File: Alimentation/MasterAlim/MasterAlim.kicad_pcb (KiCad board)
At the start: 2 copper layers, 84 parts, among them J1 Ext-Con, J10 Interf-Reg1, J11 AU Logic, J12 Interf-Reg2, J13 Interf-Reg3, J14 Interf-Reg4, J3 Bat. IN, J5 Direct Out, J6 Reg 1, J7 Reg 2, J8 Reg 3, J9 Reg 4, U1 74LS33, U2 PCF8591, U3 ACS712xLCTR-20A, U4 PCF8591, U5 PCF8591, U6 PTN78020W_EUK-7, U7 ACS712xLCTR-20A, U8 PCF8574A

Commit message: Dimensionnement et récupération des part LCSC
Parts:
- added C12: 1u, Capacitor_SMD:CP_Elec_4x5.3, F.Cu at (155.9, 131.8)
- added C14: 1n, Capacitor_SMD:C_0603_1608Metric_Pad1.08x0.95mm_HandSolder, F.Cu at (41.0, 36.5)
- added C16: 2.2u, Capacitor_SMD:C_0805_2012Metric_Pad1.18x1.45mm_HandSolder, F.Cu at (35.5, 48.5)
- added C17: 330u, Capacitor_SMD:CP_Elec_10x10, F.Cu at (38.5, 95.0)
- added C19: 1n, Capacitor_SMD:C_0603_1608Metric_Pad1.08x0.95mm_HandSolder, F.Cu at (162.5, 115.0)
- added C4: 1u, Capacitor_SMD:CP_Elec_4x5.3, F.Cu at (186.0, 123.5)
- added J2: 5V, TerminalBlock_Phoenix:TerminalBlock_Phoenix_MPT-0,5-6-2.54_1x06_P2.54mm_Horizontal, F.Cu at (34.0, 106.0)
- added REF**: MountingHole_3.2mm_M3, MountingHole:MountingHole_3.2mm_M3, F.Cu at (24.0, 106.0)
- added REF**: MountingHole_3.2mm_M3, MountingHole:MountingHole_3.2mm_M3, F.Cu at (24.0, 24.0)
- C1, C6, C9: footprint Capacitor_SMD:CP_Elec_3x5.3 -> Capacitor_SMD:CP_Elec_8x6.5
- C10, C13, C15, C18, C2, C5, C7: footprint Capacitor_SMD:C_0805_2012Metric -> Capacitor_SMD:C_0805_2012Metric_Pad1.18x1.45mm_HandSolder
- J10, J12, J13, J14: footprint Connector_JST:JST_EH_S5B-EH_1x05_P2.50mm_Horizontal -> Connector_JST:JST_PH_B5B-PH-K_1x05_P2.00mm_Vertical
- R1, R10, R11, R12, R13, R14, R15, R16, R17, R18, R19, R20, R21, R22, R23, R24, R25, R26, R27, R3, R8, R9: footprint Resistor_SMD:R_0805_2012Metric -> Resistor_SMD:R_0805_2012Metric_Pad1.20x1.40mm_HandSolder
- R2: value 150 -> 220; footprint Resistor_SMD:R_0805_2012Metric -> Resistor_SMD:R_0805_2012Metric_Pad1.20x1.40mm_HandSolder
- R28: value 150 -> 820k; footprint Resistor_SMD:R_0805_2012Metric -> Resistor_SMD:R_0805_2012Metric_Pad1.20x1.40mm_HandSolder
- R29: value 150 -> 130k; footprint Resistor_SMD:R_0805_2012Metric -> Resistor_SMD:R_0805_2012Metric_Pad1.20x1.40mm_HandSolder
- R4, R5, R6, R7: value 150 -> 180; footprint Resistor_SMD:R_0805_2012Metric -> Resistor_SMD:R_0805_2012Metric_Pad1.20x1.40mm_HandSolder
- RV1: footprint Potentiometer_THT:Potentiometer_Bourns_3299Y_Vertical -> Potentiometer_SMD:Potentiometer_Bourns_TC33X_Vertical
- U6: footprint Module:Texas_EUK_R-PDSS-T7_THT -> ARIG:Texas_EUK_R-PDSS-T7_THT
- moved R28 85.0 mm to (39.5, 43.0)
- moved J3 82.2 mm to (28.5, 33.4), turned to 270 degrees
- moved U1 81.8 mm to (159.9, 42.1)
- moved C1 74.5 mm to (182.3, 99.7)
- moved C8 74.5 mm to (184.0, 58.1)
- moved JP2 74.5 mm to (198.4, 93.1)
- moved JP3 74.5 mm to (205.2, 87.2)
- moved JP7 74.5 mm to (206.9, 45.6)
- moved JP8 74.5 mm to (200.1, 51.5)
- moved R12 74.5 mm to (200.5, 23.2)
- moved R16 74.5 mm to (192.0, 35.1)
- moved C3 74.5 mm to (195.2, 87.9)
- moved C9 74.5 mm to (183.0, 78.1)
- moved D7 74.5 mm to (196.1, 23.3)
- moved JP1 74.5 mm to (196.7, 98.0)
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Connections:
- F1 pad 2: Net-(F1-Pad2) -> /BAT_IN
- F2 pad 1: Net-(C17-Pad1) -> +5V
- R28 pad 1: Net-(J3-Pad2) -> /BAT_IN
- U3 pad 3: Net-(F1-Pad2) -> /BAT_IN
- U3 pad 4: Net-(F1-Pad2) -> /BAT_IN
- U7 pad 1: Net-(F2-Pad2) -> Net-(C17-Pad1)
- U7 pad 2: Net-(F2-Pad2) -> Net-(C17-Pad1)
- U7 pad 3: +5V -> Net-(F2-Pad2)
- U7 pad 4: +5V -> Net-(F2-Pad2)
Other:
- board outline added: 60 x 90 mm
- copper layers 2 -> 4

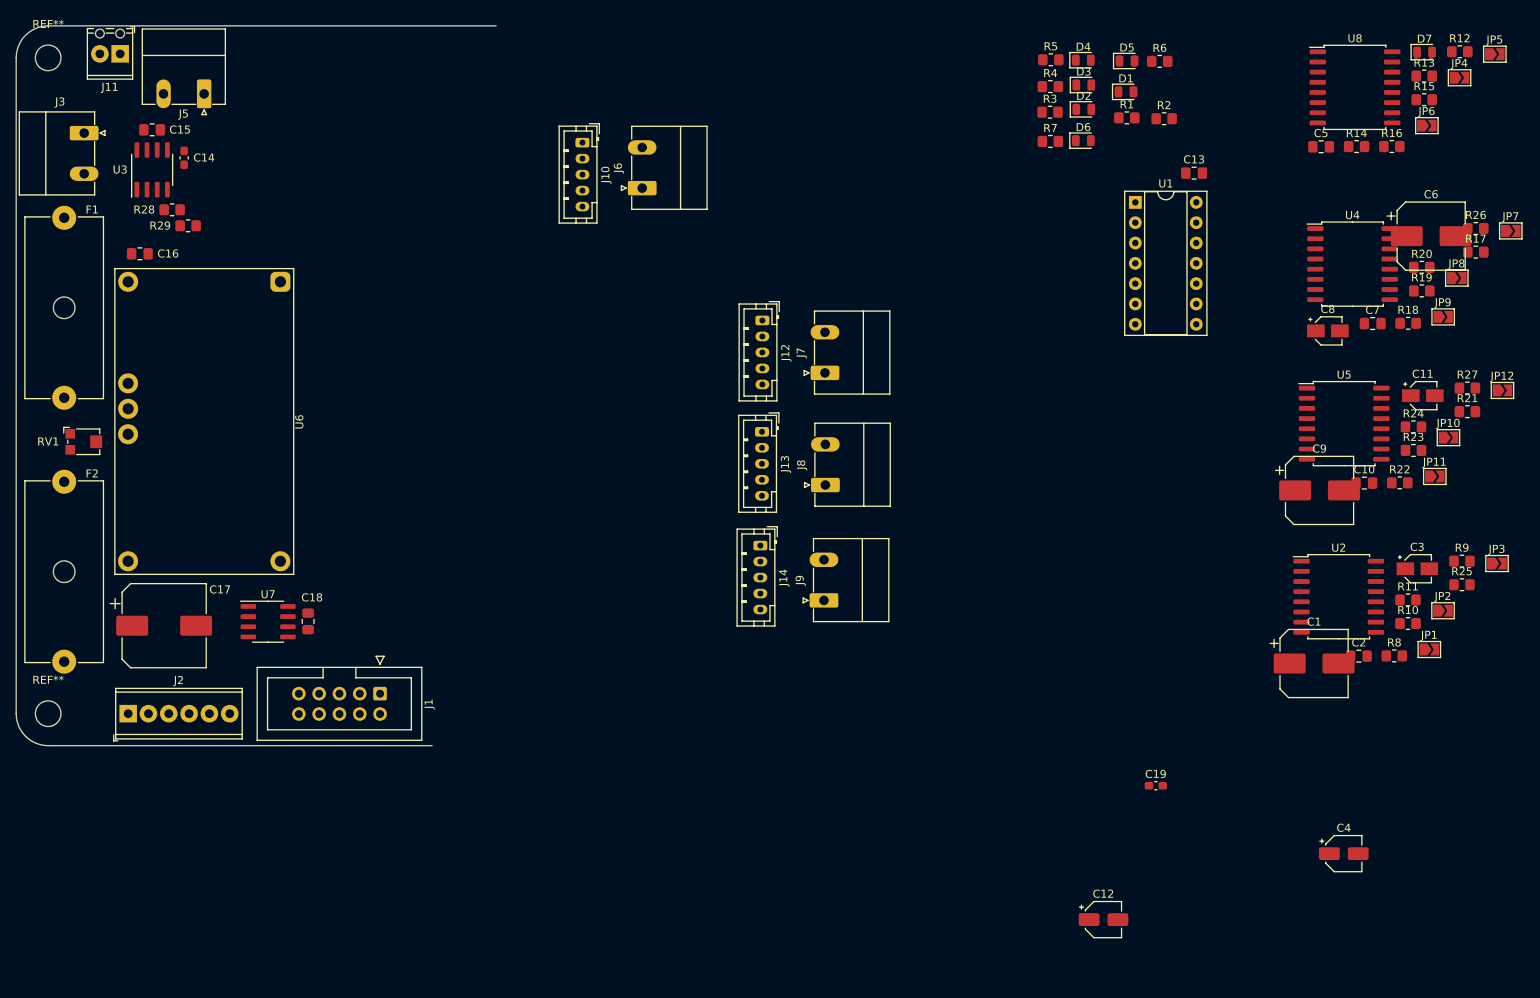
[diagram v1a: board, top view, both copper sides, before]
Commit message: Finalisation routage carte alim maitre
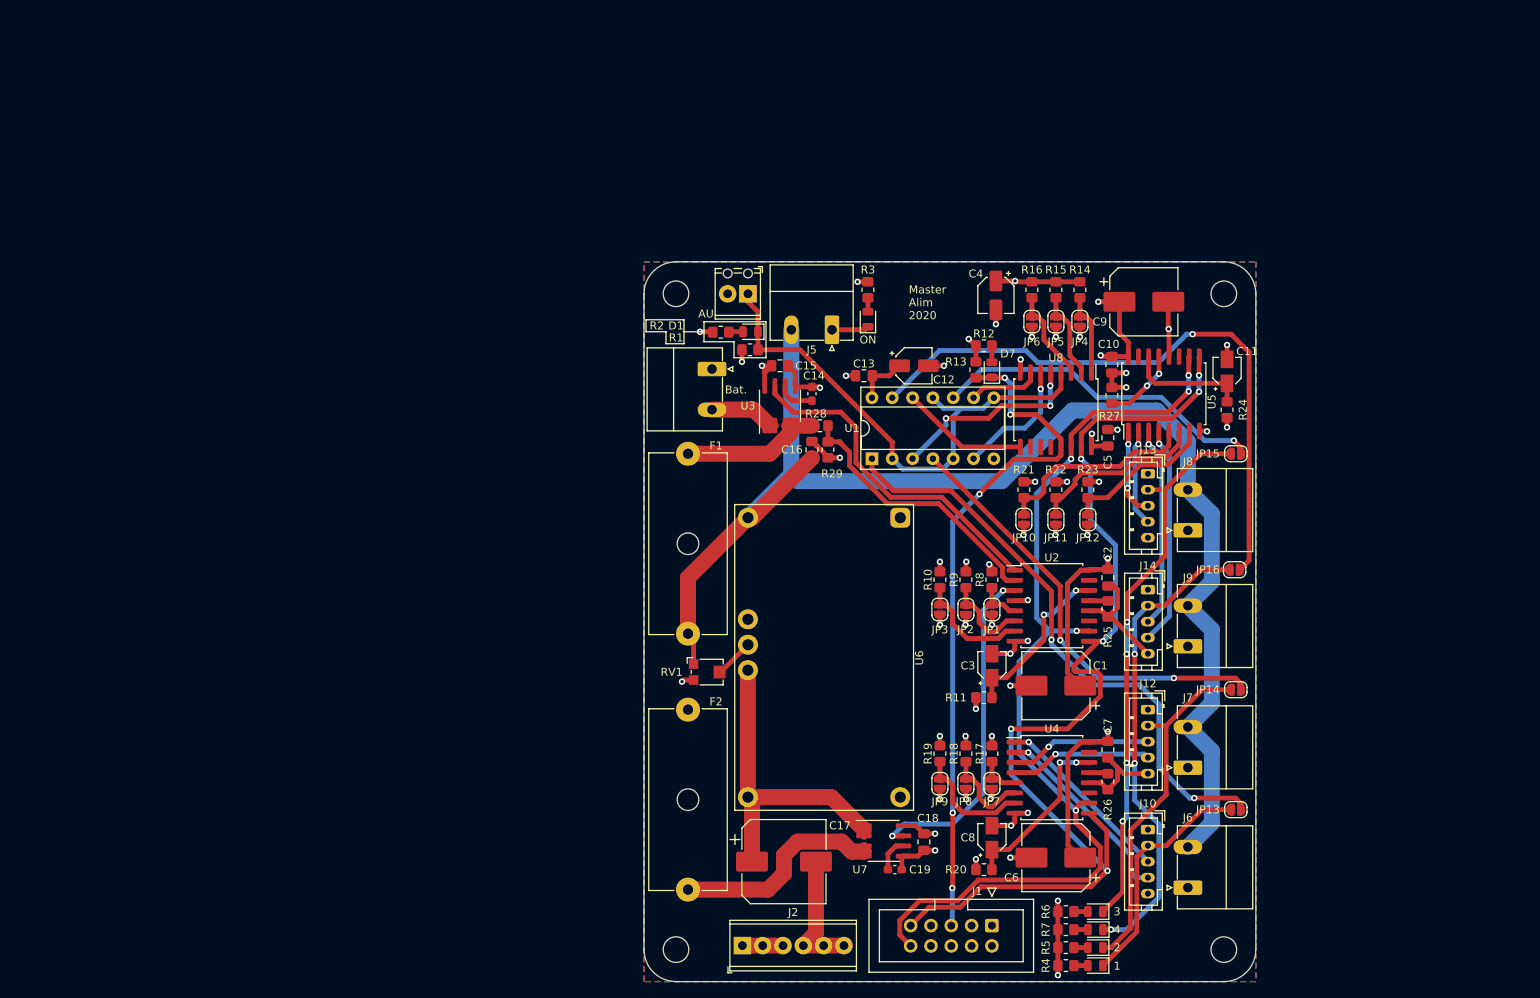
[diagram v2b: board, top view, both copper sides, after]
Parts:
- removed REF** (x2): MountingHole_3.2mm_M3, MountingHole:MountingHole_3.2mm_M3
- added H1: MountingHole, MountingHole:MountingHole_3.2mm_M3, F.Cu at (102.5, 53.5)
- added H2: MountingHole, MountingHole:MountingHole_3.2mm_M3, F.Cu at (102.5, 135.5)
- added H3: MountingHole, MountingHole:MountingHole_3.2mm_M3, F.Cu at (171.0, 53.5)
- added H4: MountingHole, MountingHole:MountingHole_3.2mm_M3, F.Cu at (171.0, 135.5)
- added JP13: EN_T1, Jumper:SolderJumper-2_P1.3mm_Open_RoundedPad1.0x1.5mm, F.Cu at (172.5, 118.0)
- added JP14: EN_T2, Jumper:SolderJumper-2_P1.3mm_Open_RoundedPad1.0x1.5mm, F.Cu at (172.5, 103.0)
- added JP15: EN_T3, Jumper:SolderJumper-2_P1.3mm_Open_RoundedPad1.0x1.5mm, F.Cu at (172.5, 73.5)
- added JP16: EN_T4, Jumper:SolderJumper-2_P1.3mm_Open_RoundedPad1.0x1.5mm, F.Cu at (172.3, 88.0)
- JP1, JP10, JP11, JP12, JP2, JP3, JP4, JP5, JP6, JP7, JP8, JP9: footprint Jumper:SolderJumper-2_P1.3mm_Open_TrianglePad1.0x1.5mm -> Jumper:SolderJumper-2_P1.3mm_Open_RoundedPad1.0x1.5mm
- R12: value 150 -> 220
- moved J10 111.3 mm to (161.5, 120.5)
- moved R5 111.0 mm to (151.2, 135.2)
- moved D4 111.0 mm to (154.9, 135.2), turned to 180 degrees
- moved J6 110.9 mm to (166.5, 127.8)
- moved D3 110.1 mm to (154.9, 137.5), turned to 180 degrees
- moved R4 109.9 mm to (151.2, 137.5)
- moved R6 107.0 mm to (151.2, 130.8)
- moved D5 106.4 mm to (154.9, 130.8), turned to 180 degrees
- moved D6 98.7 mm to (154.9, 133.0), turned to 180 degrees
- moved R7 98.6 mm to (151.2, 133.0)
- moved JP7 94.8 mm to (142.0, 114.8), turned to 270 degrees
- moved R20 93.1 mm to (141.0, 125.5)
- moved C6 90.8 mm to (150.0, 124.0), turned to 180 degrees
- moved JP8 88.1 mm to (138.8, 114.8), turned to 270 degrees
- moved C16 87.5 mm to (119.5, 73.0), turned to 90 degrees
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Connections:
- U1 pad 1: /EN_T1 -> Net-(JP13-Pad1)
- U1 pad 10: /EN_T3 -> Net-(JP15-Pad1)
- U1 pad 13: /EN_T4 -> Net-(JP16-Pad1)
- U1 pad 4: /EN_T2 -> Net-(JP14-Pad1)
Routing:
- net +BATT: track 0.00 -> 171.9 mm
- net SDA: track 0.00 -> 134.1 mm, vias 0 -> 6
- net +5V: track 0.00 -> 124.0 mm, vias 0 -> 27
- net SCL: track 0.00 -> 122.4 mm, vias 0 -> 5
- net GND: track 0.00 -> 120.8 mm, vias 0 -> 32
- net /IRQ: track 0.00 -> 85.8 mm, vias 0 -> 5
- net Net-(JP16-Pad1): track 0.00 -> 77.8 mm, vias 0 -> 1
- net Net-(JP13-Pad1): track 0.00 -> 74.0 mm, vias 0 -> 2
- net /EN_T3: track 0.00 -> 68.2 mm, vias 0 -> 4
- net /AU: track 0.00 -> 66.2 mm
- net /EN_T4: track 0.00 -> 59.1 mm, vias 0 -> 3
- net Net-(JP14-Pad1): track 0.00 -> 54.9 mm, vias 0 -> 2
- net /EN_T2: track 0.00 -> 43.8 mm
- net /ANA_5V_CURRENT: track 0.00 -> 42.8 mm, vias 0 -> 2
- net /ANA_BAT_CURRENT: track 0.00 -> 42.7 mm
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- added copper zone on In2.Cu, net +5V
- added copper zone on B.Cu, net GND
- added copper zone on F.Cu, net GND
- added copper zone on In1.Cu, net GND
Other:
- board size 60 x 90 mm -> 76.5 x 90 mm
- net class BattLipo removed
- board text added: "Master Alim 2020"
